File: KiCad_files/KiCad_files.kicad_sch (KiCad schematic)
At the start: 87 parts, among them J10 Conn_01x02_Socket, J11 MB1, J12 MB2, J13 MB1, J14 MB1, J15 MB1, J16 MB2, J17 MB1, J18 MB2, J19 MB2, J3 Conn_01x03_Socket, J6 Conn_01x01_Socket, J7 Conn_01x01_Socket, J8 Conn_01x01_Socket, J9 Conn_01x01_Socket, SW1 WE430182070816, U2 ADM3488ExR, U3 LM22670QMR-5.0, U4 MC33275ST-3.3T3G, U6 LT1789

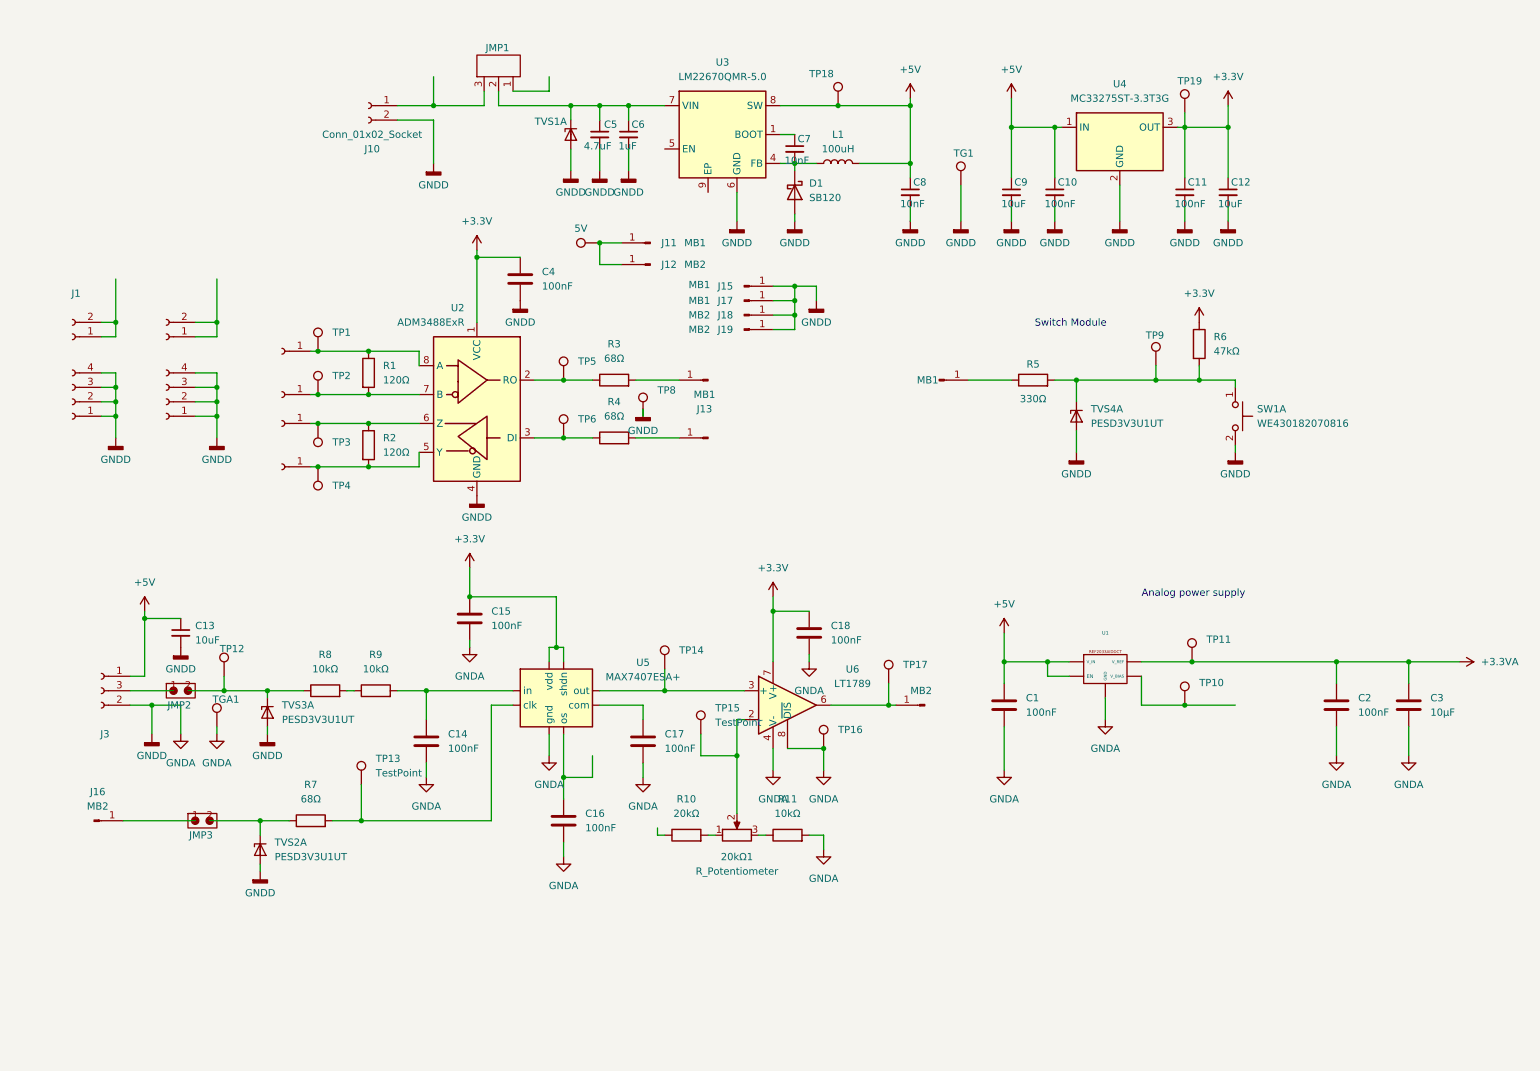
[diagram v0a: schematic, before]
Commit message: i fixed all of the errors from the schematic design
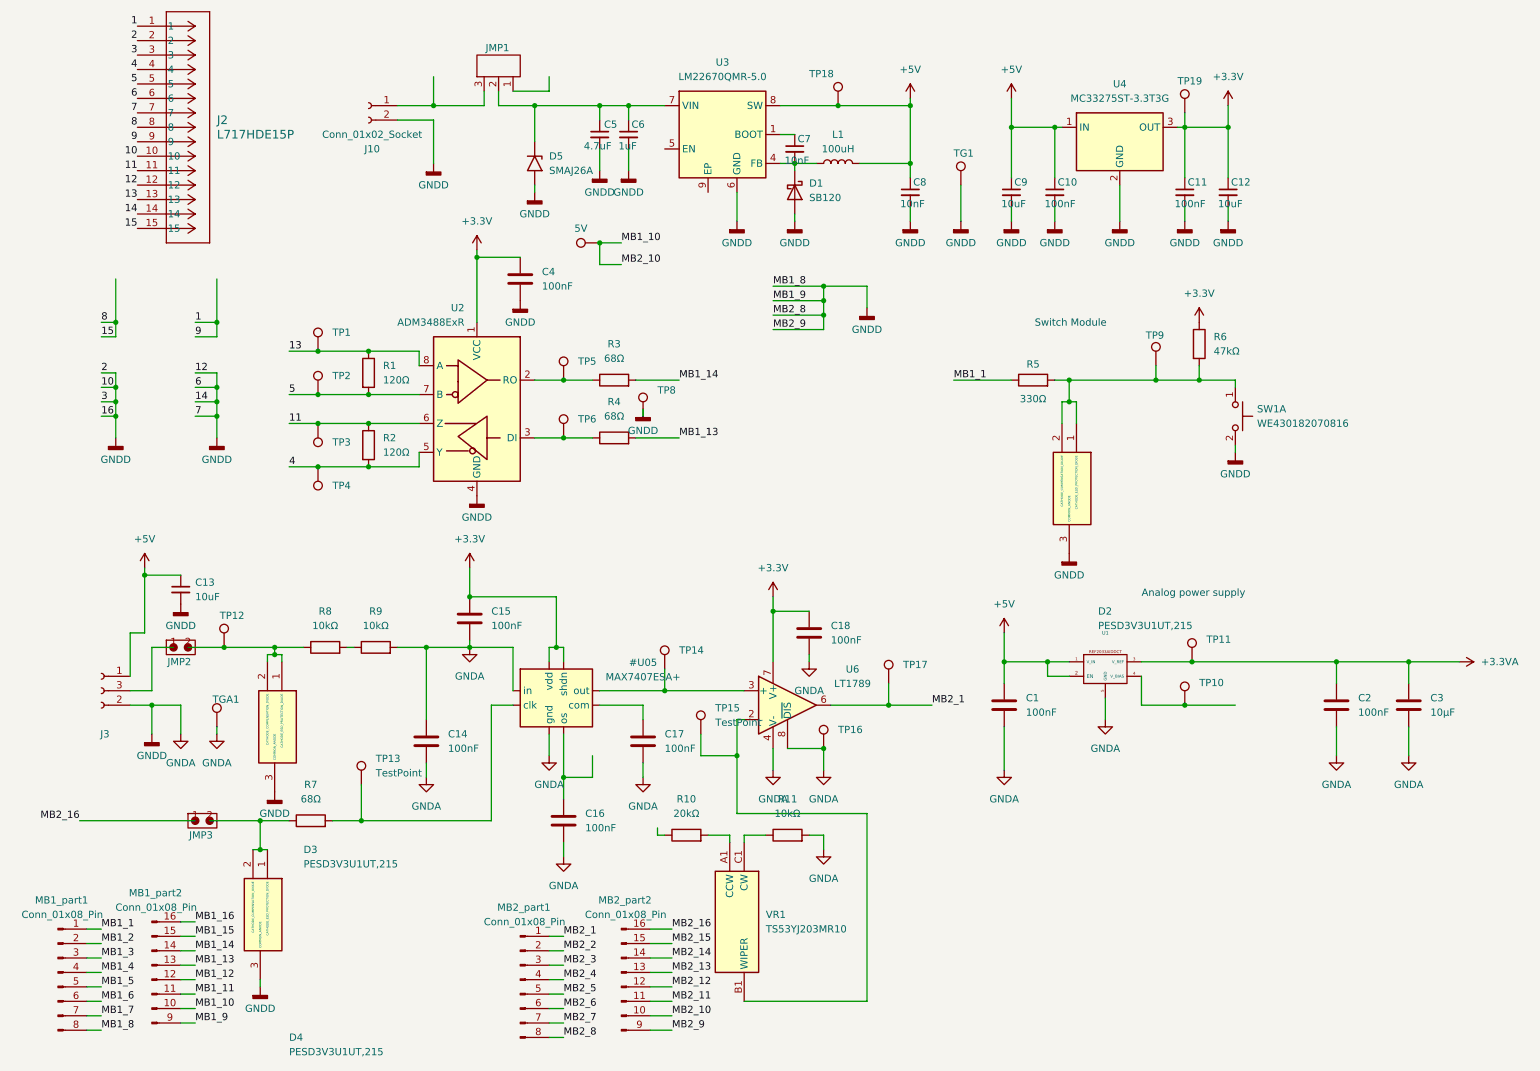
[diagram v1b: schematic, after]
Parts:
- removed 20kΩ1: R_Potentiometer, symbol Device:R_Potentiometer
- removed J1, J4: ~, symbol Connector:Conn_01x02_Socket
- removed J11, J13, J14, J15, J17: MB1, symbol Connector:Conn_01x01_Pin
- removed J12, J16, J18, J19: MB2, symbol Connector:Conn_01x01_Pin
- removed J2, J5: ~, symbol Connector:Conn_01x04_Socket
- removed J6, J7, J8, J9: Conn_01x01_Socket, symbol Connector:Conn_01x01_Socket
- removed MB1: ~, symbol Connector:Conn_01x01_Pin
- removed MB2: Conn_01x01_Pin, symbol Connector:Conn_01x01_Pin
- removed TVS1, TVS2, TVS3, TVS4: PESD3V3U1UT, Package_TO_SOT_SMD:SOT-23, symbol Power_Protection:PESD3V3L4UF
- added D2, D3, D4: PESD3V3U1UT,215, SOT95P230X110-3N, symbol New_Library:PESD3V3U1UT,215
- added D5: SMAJ26A, Diode_SMD:D_SMA, symbol Diode:SMAJ26A
- added J2: L717HDE15P, Connector_FFC-FPC:Hirose_FH26-15S-0.3SHW_2Rows-15Pins-1MP_P0.60mm_Horizontal, symbol New_Library:L717HDE15P
- added MB1_part1, MB2_part1: Conn_01x08_Pin, Library:MB1x8Pins, symbol Connector:Conn_01x08_Pin
- added MB1_part2, MB2_part2: Conn_01x08_Pin, Library:MB1x8Pins_part2, symbol Connector:Conn_01x08_Pin
- added VR1: TS53YJ203MR10, TS53YJ203MR10, symbol New_Library:TS53YJ203MR10
- C13: footprint (none) -> Capacitor_SMD:C_1210_3225Metric_Pad1.33x2.70mm_HandSolder
- C14, C15, C16, C17, C18, C4: footprint (none) -> Capacitor_SMD:C_1206_3216Metric_Pad1.33x1.80mm_HandSolder
- J10: footprint (none) -> Library:SL35290G
- J3: footprint (none) -> Library:Pin_Header_1x3_P2.54mm
- SW1: footprint MyLibrary1:Switch WE430182070816 -> Library:Switch WE430182070816
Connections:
- net +3.3VA: now also U1.3 (V_REF); no longer U1. (V_REF)
- net +5V: now also U1.1 (V_IN), U1.2 (EN); no longer U1. (V_REF)
- net GNDA: now also C14.1, R9.2, U1.5 (GND), D2.3 (COMMON_ANODE), D3.3 (COMMON_ANODE), D4.3 (COMMON_ANODE), D5.2 (A2), J2.10, J2.12, J2.14, J2.2, J2.3, J2.6, J2.7, MB1_part1.8 (Pin_8), MB1_part2.9 (Pin_8), MB2_part1.8 (Pin_8), MB2_part2.9 (Pin_8); no longer U1. (V_REF)
- net 13: now reaches R1.1, TP1.1, U2.8 (A)
- net 13: now also J2.13
- net at JMP3.2, R7.1: now also D4.1 (CATHODE_ESD_PROTECTION_DIODE), D4.2 (CATHODE_COMPENSATION_DIODE)
- net at R5.2, R6.2, SW1.1 (C)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: now also D2.1 (CATHODE_ESD_PROTECTION_DIODE), D2.2 (CATHODE_COMPENSATION_DIODE)
- net at JMP2.2, R8.1, TP12.1: now also D3.1 (CATHODE_ESD_PROTECTION_DIODE), D3.2 (CATHODE_COMPENSATION_DIODE)
- net 11: now reaches R2.1, TP3.1, U2.6 (Z)
- net 11: now also J2.11
- net 4: now reaches R2.2, TP4.1, U2.5 (Y)
- net 4: now also J2.4
- net MB2_1: now reaches TP17.1, U6.6
- net MB2_1: now also MB2_part1.1 (Pin_1)
- net MB1_14: now reaches R3.2
- net MB1_14: now also MB1_part2.14 (Pin_3)
- net MB2_16: now reaches JMP3.1
- net MB2_16: now also MB2_part2.16 (Pin_1)
- net MB1_1: now reaches R5.1
- net MB1_1: now also MB1_part1.1 (Pin_1)
- net MB1_10: now reaches TP7.1
- net MB1_10: now also MB1_part2.10 (Pin_7), MB2_part2.10 (Pin_7)
- net at TP10.1: now also U1.4 (V_BIAS); no longer U1. (V_REF)
- net at TP15.1, U6.2 (-): now also VR1.B1 (WIPER)
- net at C5.1, C6.1, JMP1.2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: now also D5.1 (A1)
- net at R11.1: now also VR1.C1 (CW)
- net 5: now reaches R1.2, TP2.1, U2.7 (B)
- net 5: now also J2.5
- net at R10.2: now also VR1.A1 (CCW)
- net MB1_13: now reaches R4.2
- net MB1_13: now also MB1_part2.13 (Pin_4)
- new net 1: J2.1, J2.9
- new net 15: J2.15, J2.8
- new net MB1_11: MB1_part2.11 (Pin_6)
- new net MB1_12: MB1_part2.12 (Pin_5)
- new net MB1_15: MB1_part2.15 (Pin_2)
- new net MB1_16: MB1_part2.16 (Pin_1)
- new net MB1_2: MB1_part1.2 (Pin_2)
- new net MB1_3: MB1_part1.3 (Pin_3)
- new net MB1_4: MB1_part1.4 (Pin_4)
- new net MB1_5: MB1_part1.5 (Pin_5)
- new net MB1_6: MB1_part1.6 (Pin_6)
- new net MB1_7: MB1_part1.7 (Pin_7)
- new net MB2_11: MB2_part2.11 (Pin_6)
- new net MB2_12: MB2_part2.12 (Pin_5)
- new net MB2_13: MB2_part2.13 (Pin_4)
- new net MB2_14: MB2_part2.14 (Pin_3)
- new net MB2_15: MB2_part2.15 (Pin_2)
- new net MB2_2: MB2_part1.2 (Pin_2)
- new net MB2_3: MB2_part1.3 (Pin_3)
- new net MB2_4: MB2_part1.4 (Pin_4)
- new net MB2_5: MB2_part1.5 (Pin_5)
- new net MB2_6: MB2_part1.6 (Pin_6)
- new net MB2_7: MB2_part1.7 (Pin_7)
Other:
- moved on the sheet: C13, JMP2, R8, R9, TP12

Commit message: fixed references and labels
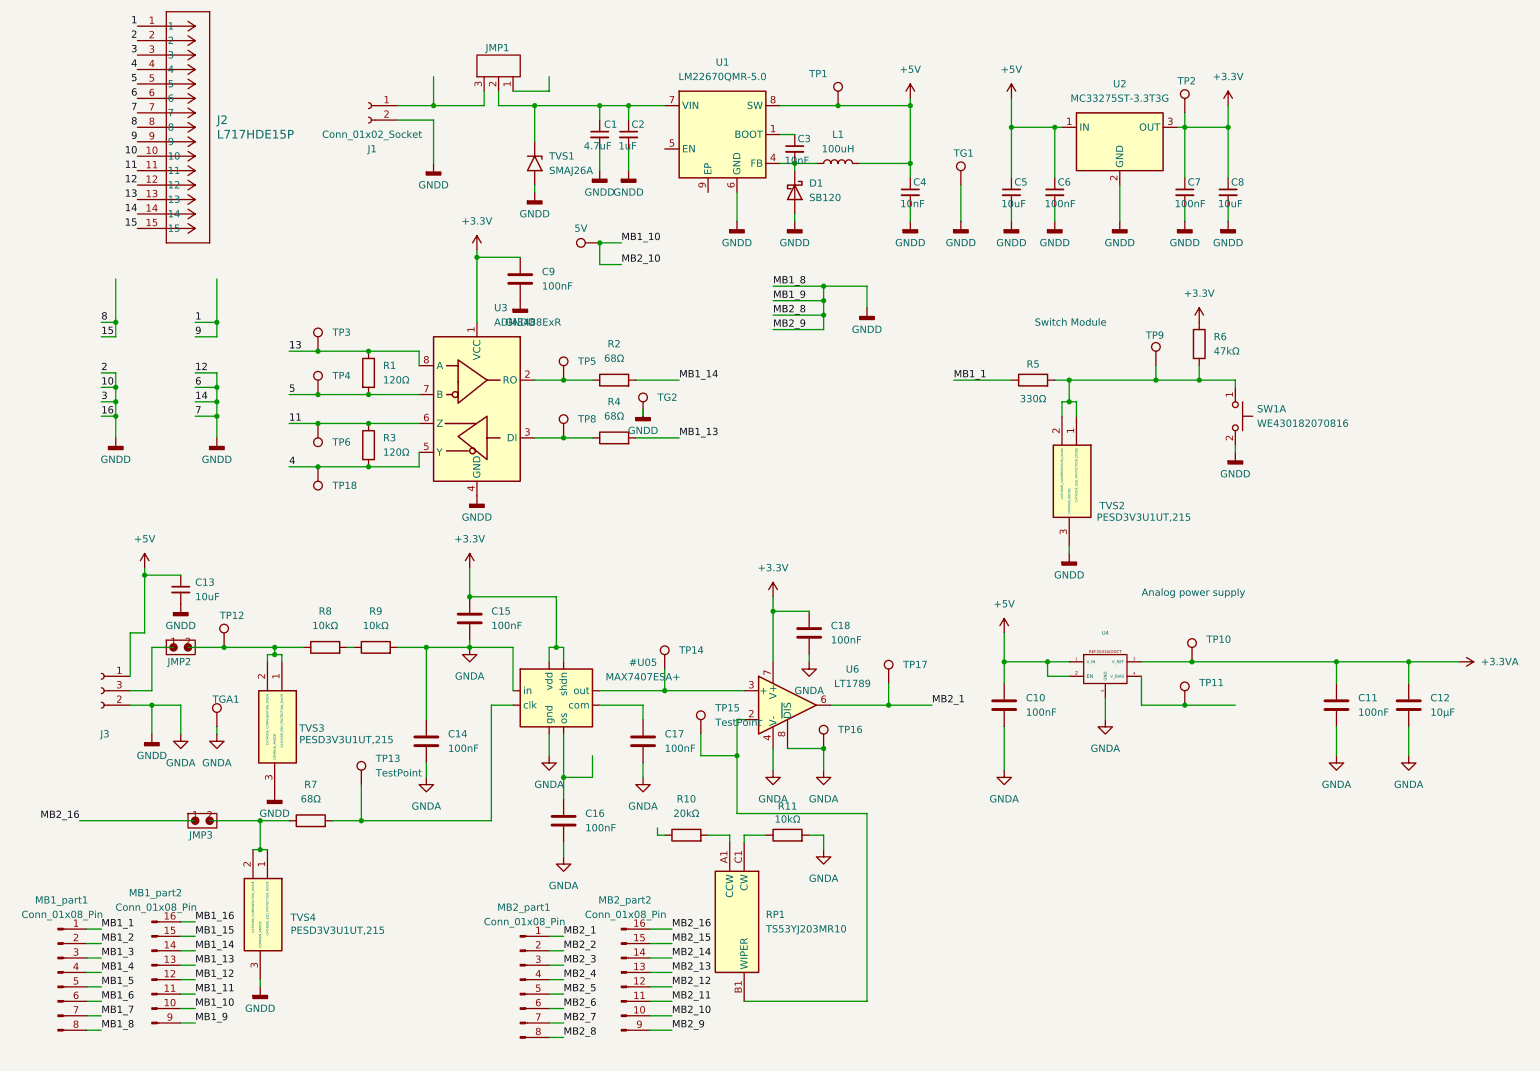
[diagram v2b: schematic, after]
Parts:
- removed TP4: TestPoint, Library:testpoint_1.4mm, symbol Connector:TestPoint
- added TP18: TestPoint, Library:testpoint_1.4mm, symbol Connector:TestPoint
- renumbered C5 to C1, C1 to C10, C2 to C11, C3 to C12, C6 to C2, C7 to C3, C8 to C4, C9 to C5, C10 to C6, C11 to C7, C12 to C8, C4 to C9, J10 to J1, R3 to R2, R2 to R3, VR1 to RP1, TP8 to TG2, TP18 to TP1, TP11 to TP10, TP10 to TP11, TP19 to TP2, TP1 to TP3, TP2 to TP4, TP3 to TP6, TP6 to TP8, D5 to TVS1, D2 to TVS2, D3 to TVS3, D4 to TVS4, U3 to U1, U4 to U2, U2 to U3, U1 to U4
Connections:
- net 4: now also TP18.1
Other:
- moved on the sheet: TVS2

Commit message: fixed pcb design details
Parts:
- D1: footprint Diode_THT:D_DO-41_SOD81_P10.16mm_Horizontal -> Diode_SMD:D_MicroSMP_AK
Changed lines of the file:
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@@
 			)
 		)
-		(property "Footprint" "Diode_THT:D_DO-41_SOD81_P10.16mm_Horizontal"
+		(property "Footprint" "Diode_SMD:D_MicroSMP_AK"
 			(at 144.145 48.26 0)
 			(effects

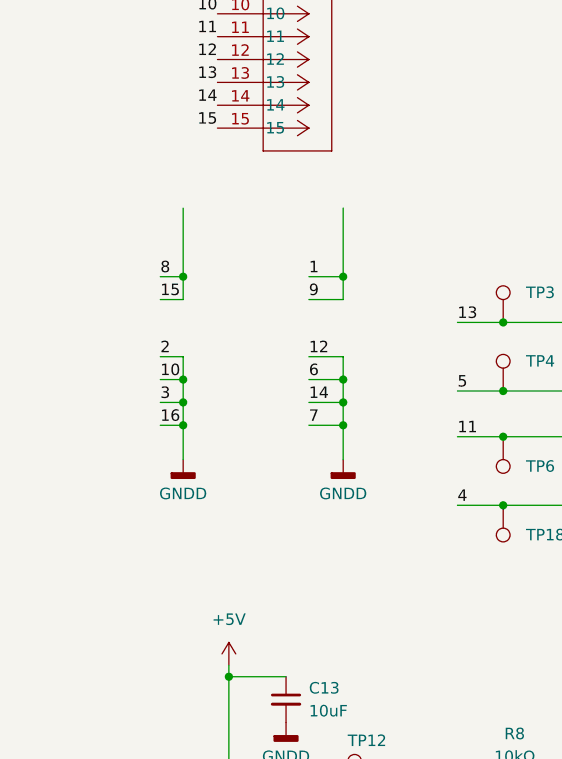
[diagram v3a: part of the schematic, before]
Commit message: Added schematic model to 15pindsub
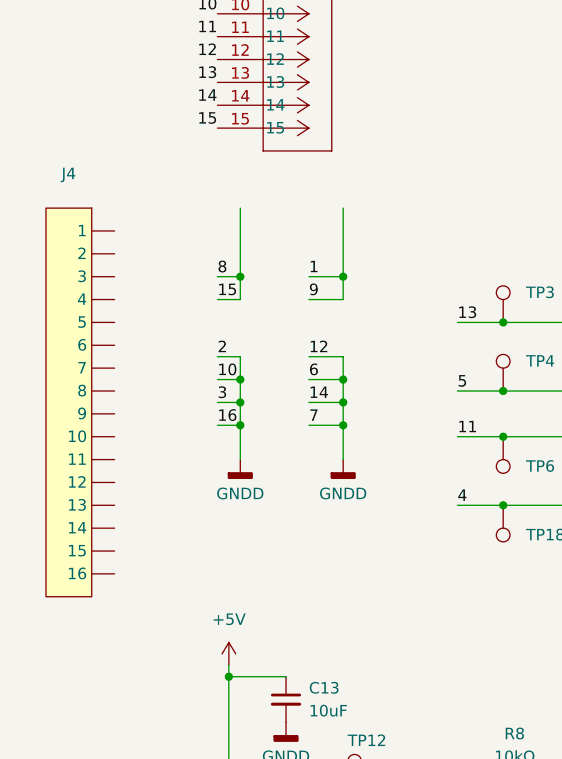
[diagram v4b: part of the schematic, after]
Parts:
- added J4: ~, Library:15PinDsub, symbol New_Library:15pinDsub

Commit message: Minor work on the PCB
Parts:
- removed J4: ~, Library:15PinDsub, symbol New_Library:15pinDsub
- added JP1: SolderJumper_2_Open, Jumper:SolderJumper-2_P1.3mm_Open_RoundedPad1.0x1.5mm, symbol Jumper:SolderJumper_2_Open
- J2: footprint Connector_FFC-FPC:Hirose_FH26-15S-0.3SHW_2Rows-15Pins-1MP_P0.60mm_Horizontal -> Library:15PinDsub
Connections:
- net GNDA: now also JP1.2 (B); no longer C1.2, C13.2, C2.2, C4.2, C5.2, C6.2, C7.2, C8.2, C9.2, D1.2 (A), J1.2 (Pin_2), J2.10, J2.12, J2.14, J2.2, J2.3, J2.6, J2.7, J3.2 (Pin_3), MB1_part1.8 (Pin_8), MB1_part2.9 (Pin_8), MB2_part1.8 (Pin_8), MB2_part2.9 (Pin_8), SW1.2 (D), TG1.1, TG2.1, TVS1.2 (A2), TVS2.3 (COMMON_ANODE), TVS3.3 (COMMON_ANODE), TVS4.3 (COMMON_ANODE), U1.6 (GND), U2.2 (GND), U3.4 (GND)
- new net GNDD: C1.2, C13.2, C2.2, C4.2, C5.2, C6.2, C7.2, C8.2, C9.2, D1.2 (A), J1.2 (Pin_2), J2.10, J2.12, J2.14, J2.16, J2.2, J2.3, J2.6, J2.7, J3.2 (Pin_3), JP1.1 (A), MB1_part1.8 (Pin_8), MB1_part2.9 (Pin_8), MB2_part1.8 (Pin_8), MB2_part2.9 (Pin_8), SW1.2 (D), TG1.1, TG2.1, TVS1.2 (A2), TVS2.3 (COMMON_ANODE), TVS3.3 (COMMON_ANODE), TVS4.3 (COMMON_ANODE), U1.6 (GND), U2.2 (GND), U2.4 (GND), U3.4 (GND)

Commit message: Updated some of the PCB
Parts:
- J3: footprint Library:Pin_Header_1x3_P2.54mm -> Library:Pin_Header_1x3_P3.5mm
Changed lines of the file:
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@@
 			)
 		)
-		(property "Footprint" "Library:Pin_Header_1x3_P2.54mm"
+		(property "Footprint" "Library:Pin_Header_1x3_P3.5mm"
 			(at 26.67 135.89 0)
 			(effects

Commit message: Significant progress on the PCB
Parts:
- added U5: ~, Package_SO:SOIC-8_3.9x4.9mm_P1.27mm, symbol New_Library:max7407esa+
- D1: footprint Diode_SMD:D_MicroSMP_AK -> Diode_THT:D_DO-41_SOD81_P10.16mm_Horizontal
- RP1: footprint TS53YJ203MR10 -> Library:TS53YJ
- U1: footprint Package_SO:SOIC-8-1EP_3.9x4.9mm_P1.27mm_EP2.29x3mm -> Package_SO:TI_SO-PowerPAD-8
- U2: footprint Package_TO_SOT_SMD:SOT-223 -> Package_TO_SOT_SMD:SOT-223-3_TabPin2
- renumbered R10 to R11, R11 to R12
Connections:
- net +3.3V: now also U5. (vdd)
- net GNDA: now also J3.3 (Pin_3), U5. (vdd); no longer JP1.2 (B)
- net GNDD: now also MB1_part2.8 (Pin_8), MB2_part2.8 (Pin_8); no longer J3.2 (Pin_3), JP1.1 (A), MB1_part2.9 (Pin_8), MB2_part2.9 (Pin_8), U2.4 (GND)
- net MB1_10: now also MB1_part2.7 (Pin_7), MB2_part2.7 (Pin_7); no longer MB1_part2.10 (Pin_7), MB2_part2.10 (Pin_7)
- net MB1_11: now also MB1_part2.6 (Pin_6); no longer MB1_part2.11 (Pin_6)
- net MB1_12: now also MB1_part2.5 (Pin_5); no longer MB1_part2.12 (Pin_5)
- net MB1_13: now also MB1_part2.4 (Pin_4); no longer MB1_part2.13 (Pin_4)
- net MB1_14: now also MB1_part2.3 (Pin_3); no longer MB1_part2.14 (Pin_3)
- net MB1_15: now also MB1_part2.2 (Pin_2); no longer MB1_part2.15 (Pin_2)
- net MB1_16: now also MB1_part2.1 (Pin_1); no longer MB1_part2.16 (Pin_1)
- net MB2_11: now also MB2_part2.6 (Pin_6); no longer MB2_part2.11 (Pin_6)
- net MB2_12: now also MB2_part2.5 (Pin_5); no longer MB2_part2.12 (Pin_5)
- net MB2_13: now also MB2_part2.4 (Pin_4); no longer MB2_part2.13 (Pin_4)
- net MB2_14: now also MB2_part2.3 (Pin_3); no longer MB2_part2.14 (Pin_3)
- net MB2_15: now also MB2_part2.2 (Pin_2); no longer MB2_part2.15 (Pin_2)
- net MB2_16: now also MB2_part2.1 (Pin_1); no longer MB2_part2.16 (Pin_1)
- net at JMP2.1: now also J3.2 (Pin_2); no longer J3.3 (Pin_2)
- net at R7.2, TP13.1: now also U5. (vdd)
- net at TP15.1, U6.2 (-): now also RP1.2 (WIPER); no longer RP1.B1 (WIPER)
- net at TP14.1, U6.3 (+): now also U5. (vdd)
- net at C16.1: now also U5. (vdd)
- net at R12.1: now also RP1.3 (CW); no longer RP1.C1 (CW)
- net at C17.1: now also U5. (vdd)
- net at R11.2: now also RP1.1 (CCW); no longer RP1.A1 (CCW)

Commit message: Significant progress on the PCB
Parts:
- removed TP7: 5V, Library:testpoint_1.4mm, symbol Connector:TestPoint
- D1: footprint Diode_THT:D_DO-41_SOD81_P10.16mm_Horizontal -> Diode_SMD:D_MicroSMP_AK
- renumbered TP18 to TP7
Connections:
- net +3.3V: now also U5.4 (vdd), U5.7 (shdn); no longer U5. (vdd)
- net +5V: now also MB1_part2.10 (Pin_7), MB2_part2.10 (Pin_7)
- net 1: now also J1.1 (Pin_1), JMP1.3
- net 15: now also JMP1.1
- net GNDA: now also JP1.1 (A), U5.3 (gnd); no longer C14.1, R9.2, U5. (vdd)
- net GNDD: now also JP1.2 (B), MB1_part2.9 (Pin_8), MB2_part2.9 (Pin_8); no longer MB1_part2.8 (Pin_8), MB2_part2.8 (Pin_8)
- net MB1_11: now also MB1_part2.11 (Pin_6); no longer MB1_part2.6 (Pin_6)
- net MB1_12: now also MB1_part2.12 (Pin_5); no longer MB1_part2.5 (Pin_5)
- net MB1_13: now also MB1_part2.13 (Pin_4); no longer MB1_part2.4 (Pin_4)
- net MB1_14: now also MB1_part2.14 (Pin_3); no longer MB1_part2.3 (Pin_3)
- net MB1_15: now also MB1_part2.15 (Pin_2); no longer MB1_part2.2 (Pin_2)
- net MB1_16: now also MB1_part2.16 (Pin_1); no longer MB1_part2.1 (Pin_1)
- net MB2_11: now also MB2_part2.11 (Pin_6); no longer MB2_part2.6 (Pin_6)
- net MB2_12: now also MB2_part2.12 (Pin_5); no longer MB2_part2.5 (Pin_5)
- net MB2_13: now also MB2_part2.13 (Pin_4); no longer MB2_part2.4 (Pin_4)
- net MB2_14: now also MB2_part2.14 (Pin_3); no longer MB2_part2.3 (Pin_3)
- net MB2_15: now also MB2_part2.15 (Pin_2); no longer MB2_part2.2 (Pin_2)
- net MB2_16: now also MB2_part2.16 (Pin_1); no longer MB2_part2.1 (Pin_1)
- net at R7.2, TP13.1: now also U5.8 (clk); no longer U5. (vdd)
- net at TP14.1, U6.3 (+): now also U5.5 (out); no longer U5. (vdd)
- net VBIAS: now reaches C16.1
- net VBIAS: now also R11.1, TP11.1, U4.4 (V_BIAS), U5.6 (os); no longer U5. (vdd)
- net at C17.1: now also U5.1 (com); no longer U5. (vdd)
- removed net MB1_10: MB1_part2.7 (Pin_7), MB2_part2.7 (Pin_7)
- new net: C14.1, R9.2, U5.2 (in)
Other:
- moved on the sheet: C15
